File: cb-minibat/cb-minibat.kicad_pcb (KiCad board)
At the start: 4 copper layers, 25.4 x 55.8 mm, 33 parts, among them P1 CONN_01X14, P2 CONN_01X14, P3 CONN_8, SW1 SW_PUSH, U1 BMP180, U2 MAX1724, U3 SI7021, U4 M74VHC1GT08, U5 MCP1702, U6 LSM9DS0

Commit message: Fiducials added to the PCB
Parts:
- added fiducial: VAL**, mymods:fiducial, F.Cu at (153.3, 100.0)
- added fiducial: VAL**, mymods:fiducial, F.Cu at (175.2, 47.8)
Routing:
- net GND: track 83.3 -> 81.4 mm
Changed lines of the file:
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@@
-(kicad_pcb (version 4) (host pcbnew 0.201505141916+5653~23~ubuntu14.04.1-product)
+(kicad_pcb (version 4) (host pcbnew no-vcs-found-product)
   (general
     (links 123)
     (no_connects 0)
-    (area 125.889657 38.803159 184.752904 119.68226)
+    (area 144.022537 38.803159 184.752904 103.86822)
     (thickness 1.6002)
     (drawings 69)
     (tracks 840)
     (zones 0)
-    (modules 33)
+    (modules 35)
     (nets 38)
   )
@@
   )
   (setup
-    (last_trace_width 0.508)
+    (last_trace_width 0.1524)
     (user_trace_width 0.2032)
     (user_trace_width 0.254)
@@
     (add_net VCC)
   )
+  (module myconnectors:PIN_ARRAY_8X1 (layer Front)
+    (at 164.32784 100.49002)
+    (descr "Double rangee de contacts 2 x 12 pins")
+    (tags CONN)
+    (fp_text reference P3 (at -4.09448 2.35204) (layer F.SilkS) hide
+      (effects (font (size 1.016 1.016) (thickness 0.254)))
+    )
+    (fp_text value CONN_8 (at 0.381 2.413) (layer F.SilkS) hide
+      (effects (font (size 1.016 1.016) (thickness 0.2032)))
+    )
+    (pad 1 thru_hole rect (at -8.89 0) (size 1.524 1.524) (drill 0.8128) (layers *.Cu *.Mask F.SilkS)
+      (net 25 +BATT))
+    (pad 2 thru_hole circle (at -6.35 0) (size 1.524 1.524) (drill 1.016) (layers *.Cu *.Mask F.SilkS)
+      (net 2 GND))
+    (pad 3 thru_hole circle (at -3.81 0) (size 1.524 1.524) (drill 1.016) (layers *.Cu *.Mask F.SilkS)
+      (net 3 VCC))
+    (pad 4 thru_hole circle (at -1.27 0) (size 1.524 1.524) (drill 1.016) (layers *.Cu *.Mask F.SilkS)
+      (net 2 GND))
+    (pad 5 thru_hole circle (at 1.27 0) (size 1.524 1.524) (drill 1.016) (layers *.Cu *.Mask F.SilkS)
+      (net 26 +5V))
+    (pad 6 thru_hole circle (at 3.81 0) (size 1.524 1.524) (drill 1.016) (layers *.Cu *.Mask F.SilkS)
+      (net 2 GND))
+    (pad 7 thru_hole circle (at 6.35 0) (size 1.524 1.524) (drill 1.016) (layers *.Cu *.Mask F.SilkS)
+      (net 31 /5VOUT))
+    (pad 8 thru_hole circle (at 8.89 0) (size 1.524 1.524) (drill 1.016) (layers *.Cu *.Mask F.SilkS)
+      (net 2 GND))
+    (model pin_array/pins_array_12x2.wrl
+      (at (xyz 0 0 0))
+      (scale (xyz 1 1 1))
+      (rotate (xyz 0 0 0))
+    )
+  )
   (module mysmd:SM0603S (layer Front)
     (at 160.147 81.64322 90)
@@
     )
   )
-  (module myconnectors:PIN_ARRAY_8X1 (layer Front)
-    (at 164.32784 100.49002)
-    (descr "Double rangee de contacts 2 x 12 pins")
-    (tags CONN)
-    (fp_text reference P3 (at -4.09448 2.35204) (layer F.SilkS) hide
-      (effects (font (size 1.016 1.016) (thickness 0.254)))
-    )
-    (fp_text value CONN_8 (at 0.381 2.413) (layer F.SilkS) hide
-      (effects (font (size 1.016 1.016) (thickness 0.2032)))
-    )
-    (fp_line (start 10.287 1.27) (end 10.287 -1.27) (layer F.SilkS) (width 0.381))
-    (fp_line (start 10.287 -1.27) (end -10.033 -1.27) (layer F.SilkS) (width 0.381))
-    (fp_line (start -10.033 -1.27) (end -10.033 1.27) (layer F.SilkS) (width 0.381))
-    (fp_line (start -10.033 1.27) (end 10.287 1.27) (layer F.SilkS) (width 0.381))
-    (fp_line (start -10.033 1.27) (end -10.033 -1.27) (layer F.SilkS) (width 0.381))
-    (pad 1 thru_hole rect (at -8.89 0) (size 1.524 1.524) (drill 0.8128) (layers *.Cu *.Mask F.SilkS)
-      (net 25 +BATT))
-    (pad 2 thru_hole circle (at -6.35 0) (size 1.524 1.524) (drill 1.016) (layers *.Cu *.Mask F.SilkS)
-      (net 2 GND))
-    (pad 3 thru_hole circle (at -3.81 0) (size 1.524 1.524) (drill 1.016) (layers *.Cu *.Mask F.SilkS)
-      (net 3 VCC))
-    (pad 4 thru_hole circle (at -1.27 0) (size 1.524 1.524) (drill 1.016) (layers *.Cu *.Mask F.SilkS)
-      (net 2 GND))
-    (pad 5 thru_hole circle (at 1.27 0) (size 1.524 1.524) (drill 1.016) (layers *.Cu *.Mask F.SilkS)
-      (net 26 +5V))
-    (pad 6 thru_hole circle (at 3.81 0) (size 1.524 1.524) (drill 1.016) (layers *.Cu *.Mask F.SilkS)
-      (net 2 GND))
-    (pad 7 thru_hole circle (at 6.35 0) (size 1.524 1.524) (drill 1.016) (layers *.Cu *.Mask F.SilkS)
-      (net 31 /5VOUT))
-    (pad 8 thru_hole circle (at 8.89 0) (size 1.524 1.524) (drill 1.016) (layers *.Cu *.Mask F.SilkS)
-      (net 2 GND))
-    (model pin_array/pins_array_12x2.wrl
-      (at (xyz 0 0 0))
-      (scale (xyz 1 1 1))
-      (rotate (xyz 0 0 0))
-    )
-  )
   (module libcms:SM0805 (layer Front)
     (at 156.27096 91.37142)
@@
       (net 23 /I2C_SDA))
   )
+  (module mymods:fiducial (layer Front)
+    (at 153.35 99.95)
+    (fp_text reference fiducial (at -0.25 3.65) (layer F.SilkS) hide
+      (effects (font (thickness 0.3048)))
+    )
+    (fp_text value VAL** (at -0.85 5.95) (layer F.SilkS) hide
+      (effects (font (thickness 0.3048)))
+    )
+    (pad 1 smd circle (at 0 0) (size 1 1) (layers Front F.Mask)
+      (solder_mask_margin 0.5) (clearance 0.5))
+  )
+  (module mymods:fiducial (layer Front)
+    (at 175.15 47.825)
+    (fp_text reference fiducial (at 0.975 -5.475) (layer F.SilkS) hide
+      (effects (font (thickness 0.3048)))
+    )
+    (fp_text value VAL** (at 1.15 -3.45) (layer F.SilkS) hide
+      (effects (font (thickness 0.3048)))
+    )
+    (pad 1 smd circle (at 0 0) (size 1 1) (layers Front F.Mask)
+      (solder_mask_margin 0.5) (clearance 0.5))
+  )
   (gr_line (start 177.02784 48.51654) (end 177.0253 48.51654) (angle 90) (layer Edge.Cuts) (width 0.381))
   (gr_line (start 177.02784 51.05654) (end 177.02784 48.51654) (angle 90) (layer Edge.Cuts) (width 0.381))
@@
   (gr_line (start 177.02772 99.25008) (end 177.02772 78.56008) (angle 90) (layer Edge.Cuts) (width 0.381))
   (gr_line (start 151.62772 78.62008) (end 151.62772 99.72008) (angle 90) (layer Edge.Cuts) (width 0.381))
-  (gr_text "minibat\n1.0" (at 156.34772 49.50008) (layer F.SilkS)
+  (gr_text "minibat\n1.0" (at 156.4 50.625) (layer F.SilkS)
     (effects (font (size 1.27 1.143) (thickness 0.1524)))
   )
-  (gr_text "Mini battery\nboard" (at 172.38772 49.50008) (layer F.SilkS)
+  (gr_text "Mini battery\nboard" (at 172.3 50.6) (layer F.SilkS)
     (effects (font (size 1.143 0.889) (thickness 0.1524)))
   )
@@
   (segment (start 174.99772 51.30046) (end 174.88772 51.41046) (width 0.508) (layer Front) (net 2))
   (via (at 174.99772 51.30046) (size 0.6858) (layers Front Back) (net 2))
-  (segment (start 174.99772 47.74046) (end 174.99772 51.30046) (width 0.508) (layer Back) (net 2))
-  (segment (start 174.96772 47.71046) (end 174.99772 47.74046) (width 0.508) (layer Back) (net 2))
-  (via (at 174.96772 47.71046) (size 0.6858) (layers Front Back) (net 2))
-  (segment (start 171.28772 47.71046) (end 174.96772 47.71046) (width 0.508) (layer Front) (net 2))
+  (segment (start 173.73 48.98) (end 174.99772 51.30046) (width 0.508) (layer Back) (net 2))
+  (segment (start 173.7 48.95) (end 173.73 48.98) (width 0.508) (layer Back) (net 2))
+  (via (at 173.7 48.95) (size 0.6858) (layers Front Back) (net 2))
+  (segment (start 171.28772 47.71046) (end 173.7 48.95) (width 0.508) (layer Front) (net 2))
   (segment (start 171.26772 47.69046) (end 171.28772 47.71046) (width 0.508) (layer Front) (net 2))
   (via (at 171.26772 47.69046) (size 0.6858) (layers Front Back) (net 2))

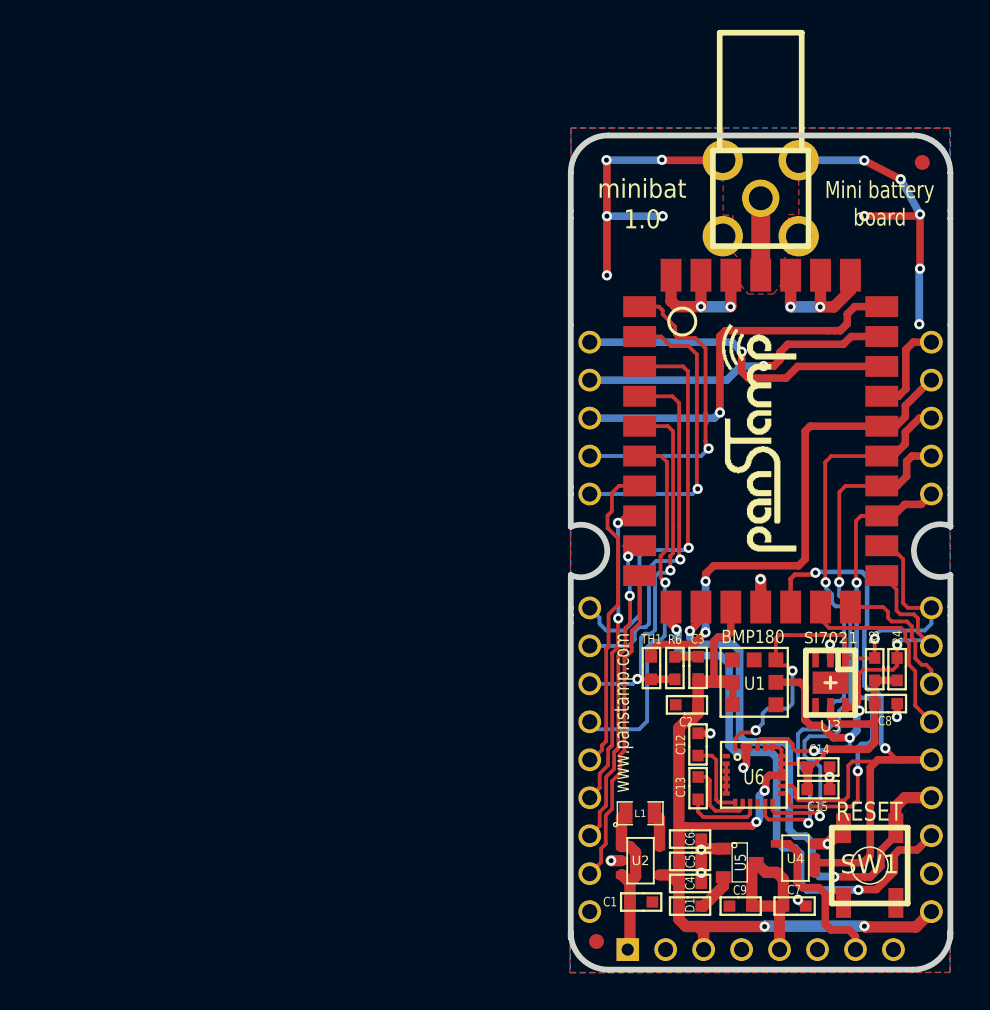
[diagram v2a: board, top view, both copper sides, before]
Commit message: Adding MMA8652 accelerometer and PCB meander antenna
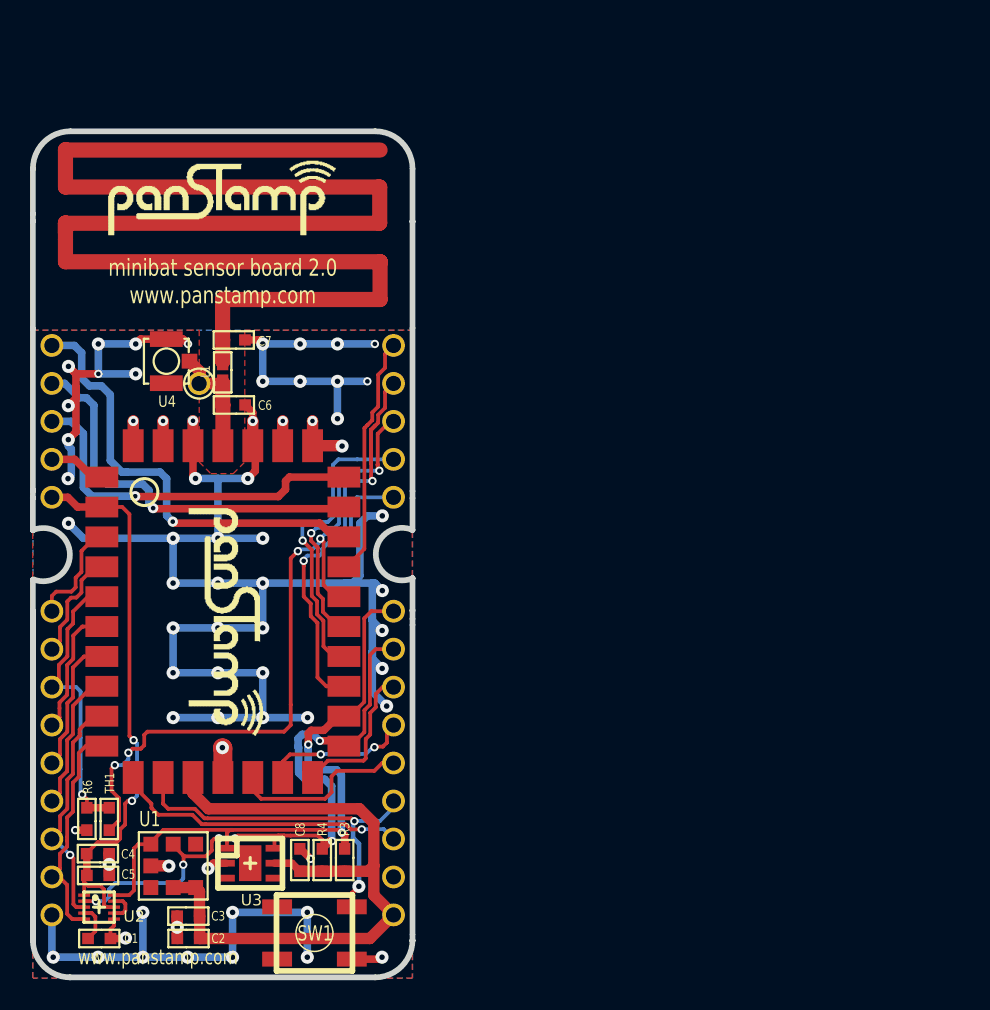
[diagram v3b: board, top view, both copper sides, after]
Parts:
- removed ANT1: ANTENNA, myconnectors:SMA_RightAngle_Tyco
- removed C12: 4.7u, mysmd:SM0603S
- removed C13: 220n, mysmd:SM0603S
- removed C14, C9: 10u, mysmd:SM0603S
- removed C15: 100n, mysmd:SM0603S
- removed D1: SD0603S040S0R2, mysmd:SM0603S
- removed the G*** at (161.4, 73.9)
- removed the G*** at (171.1, 53.7)
- removed P3: CONN_8, myconnectors:PIN_ARRAY_8X1
- removed U5: MCP1702, libcms:SOT23
- removed U6: LSM9DS0, mysmd:LGA24
- removed fiducial (x2): VAL**, mymods:fiducial
- added G***: PANSTAMPLOGO, mymods:PANSTAMPLOGO, F.Cu at (131.3, 71.0)
- added G***: PANSTAMPLOGO, mymods:PANSTAMPLOGO, F.Cu at (120.7, 47.4)
- added pin: VAL**, myconnectors:pin, F.Cu at (126.8, 62.6)
- C1: value 10u -> 100n
- C4: value 10u -> 1u
- C5: value 1u -> 100n
- C6, C7: value 100n -> N.P.
- L1: value 4.7u -> 0; footprint libcms:SM0805 -> mysmd:SM0603S
- U2: value MAX1724 -> MMA8652FC; footprint libcms:SOT23-5 -> mysmd:DFN-10
- U4: value M74VHC1GT08 -> ANTENNA; footprint libcms:SOT23-5 -> myconnectors:U.FL_CONN
- moved U4 53.6 mm to (124.6, 61.1), turned to 0 degrees
- moved C7 53.3 mm to (129.1, 59.7)
- moved C6 42.1 mm to (129.1, 64.0)
- moved U1 40.8 mm to (125.0, 94.9), turned to 0 degrees
- moved U3 40.7 mm to (130.2, 94.7), turned to 270 degrees
- moved L1 40.6 mm to (128.3, 61.9), turned to 90 degrees
- moved R6 40.6 mm to (119.2, 91.8), turned to 270 degrees
- moved C8 40.6 mm to (133.5, 94.5), turned to 90 degrees
- moved R4 40.5 mm to (135.0, 94.5)
- moved C4 39.7 mm to (120.0, 94.1)
- moved C5 39.6 mm to (120.0, 95.5)
- moved C3 37.9 mm to (126.0, 98.2), turned to 180 degrees
- moved PS1 37.7 mm to (128.4, 77.9)
- moved R3 37.7 mm to (136.5, 94.5)
- moved TH1 37.7 mm to (120.8, 91.8), turned to 270 degrees
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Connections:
- C1 pad 1: +BATT -> Net-(C1-Pad1)
- C4 pad 1: VCC -> /D16
- C5 pad 1: VCC -> /D16
- C6 pad 1: VCC -> /TOANT
- C7 pad 1: +5V -> Net-(C7-Pad1)
- L1 pad 1: +BATT -> /TOANT
- L1 pad 2: Net-(L1-Pad2) -> Net-(C7-Pad1)
- SW1 pad 1: /RESET -> GND
- SW1 pad 2: GND -> /RESET
- U2 pad 1: +BATT -> /D16
- U2 pad 2: GND -> /I2C_SCL
- U2 pad 3: +BATT -> /D9
- U2 pad 4: VCC -> Net-(C1-Pad1)
- U2 pad 5: Net-(L1-Pad2) -> /D8
- U4 pad 1: /D7 -> /TOANT
- U4 pad 2: /D7 -> GND
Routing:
- net GND: track 81.4 -> 192.3 mm, vias 26 -> 67
- net Net-(C7-Pad1): track 0.00 -> 109.8 mm
- net /D7: track 49.4 -> 13.1 mm, vias 2 -> 0
- net VCC: track 81.1 -> 46.4 mm, vias 4 -> 0
- net /D0: track 41.0 -> 20.2 mm
- net /D15: track 27.4 -> 7.20 mm, vias 1 -> 0
- net /D22: track 34.6 -> 54.2 mm, vias 2 -> 5
- net /TEST: track 38.4 -> 19.6 mm, vias 2 -> 1
- net /D17: track 21.7 -> 3.83 mm, vias 1 -> 0
- net /D14: track 24.3 -> 7.37 mm, vias 1 -> 0
- net /D16: track 20.8 -> 37.0 mm, vias 1 -> 2
- net /D12: track 25.4 -> 9.48 mm, vias 1 -> 0
- net /D1: track 36.7 -> 20.9 mm, vias 2 -> 1
- net /D2: track 34.2 -> 19.4 mm, vias 2 -> 1
- net +5V: track 12.2 -> 0.00 mm
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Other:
- board size 25.4 x 55.8 mm -> 25.4 x 56.6 mm
- net class Default: clearance 0.1524 -> 0.127; via_dia 0.6858 -> 0.5588; via_drill 0.3302 -> 0.3048
- rule trace_clearance: 0.1524 -> 0.127
- rule trace_min: 0.006 -> 0.1524
- rule via_min_drill: 0.3302 -> 0.3048
- rule via_min_size: 0.027 -> 0.5588
- board text added: "minibat sensor board 2.0 www.panstamp.com"
- board text removed: "Mini battery board"
- board text removed: "minibat 1.0"
